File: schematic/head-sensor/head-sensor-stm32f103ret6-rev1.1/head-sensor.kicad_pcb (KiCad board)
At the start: 2 copper layers, 49 parts, among them P1 MICROSD-SDIO-CD, P10 SensorsIn, P11 USART1, P12 SensorsGND, P13 RFID-RC522-MODULE, P14 NRF24L01, P15 HeadLEDs, P16 Power, P2 Vibroengines, P3 NRST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

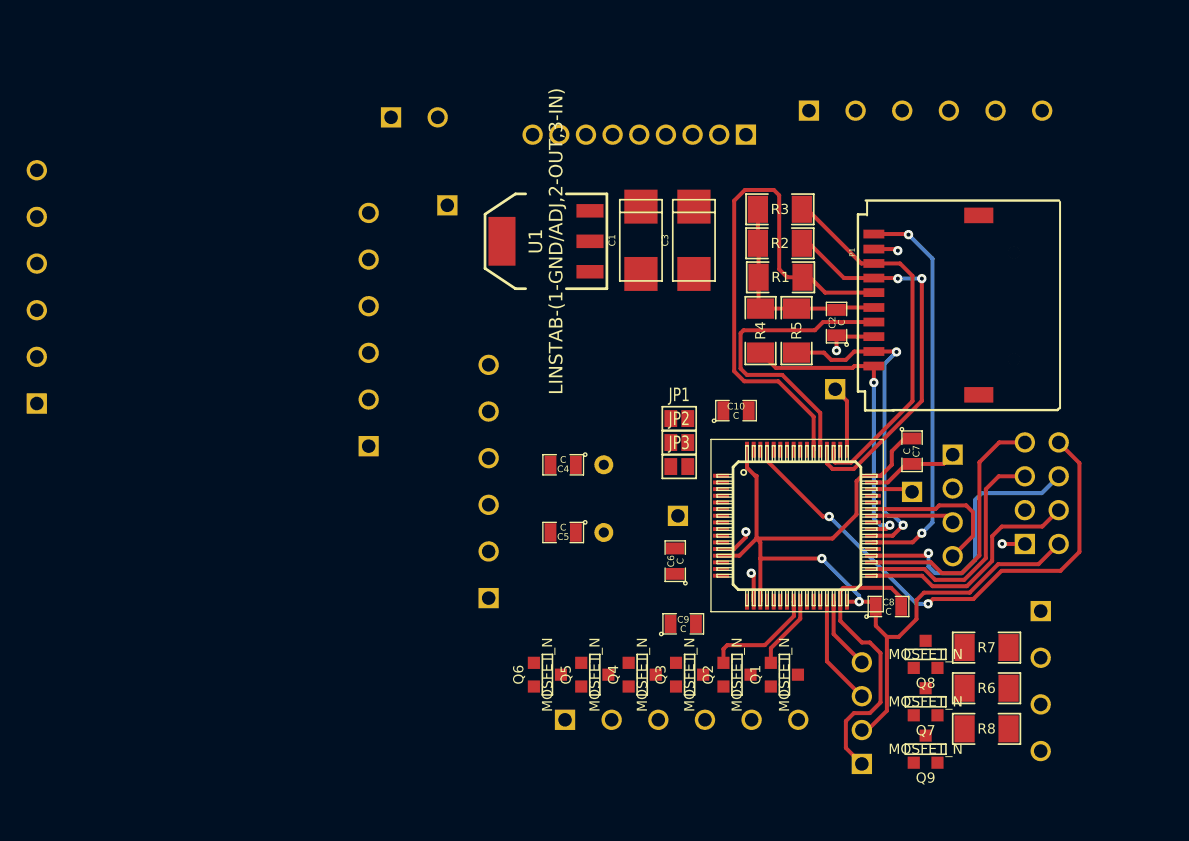
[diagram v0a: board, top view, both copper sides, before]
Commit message: Head sensor routing done
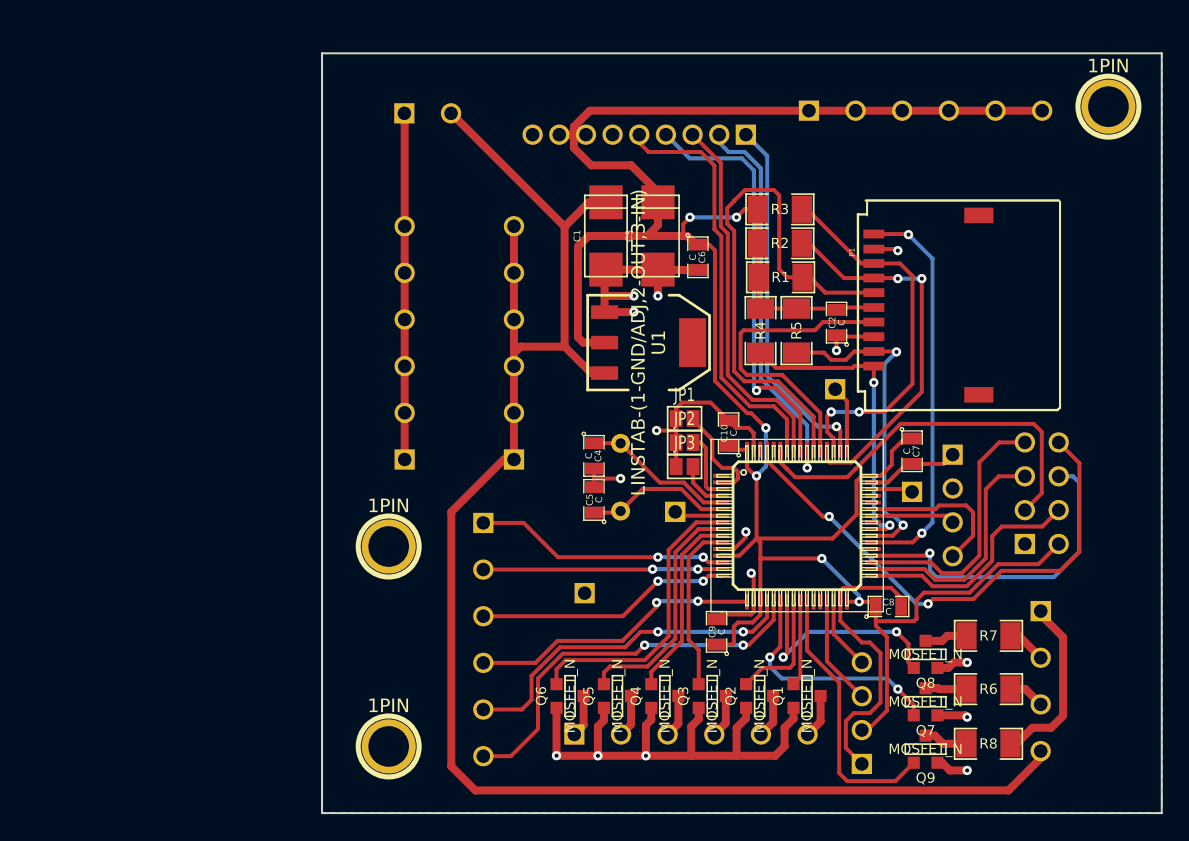
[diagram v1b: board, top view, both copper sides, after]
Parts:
- added 1PIN: P***, 1pin, F.Cu at (127.0, 60.0)
- added 1PIN: P***, 1pin, F.Cu at (73.0, 108.0)
- added 1PIN: P***, 1pin, F.Cu at (73.0, 93.0)
- moved P5 36.0 mm to (82.4, 77.7)
- moved P4 30.9 mm to (87.7, 96.5)
- moved C6 22.9 mm to (96.2, 71.3), turned to 270 degrees
- moved P10 11.9 mm to (80.1, 100.0), turned to 270 degrees
- moved U1 10.8 mm to (92.5, 77.7), turned to 270 degrees
- moved C5 3.36 mm to (88.4, 89.5), turned to 90 degrees
- moved P12 2.88 mm to (74.2, 77.7)
- moved C3 2.72 mm to (93.2, 69.7)
- moved C1 2.65 mm to (89.3, 69.7)
- moved C9 2.57 mm to (97.6, 99.4), turned to 90 degrees
- moved C4 2.40 mm to (88.4, 86.2), turned to 270 degrees
- moved Q1 2.33 mm to (104.4, 104.2)
- moved Q3 2.33 mm to (97.3, 104.2)
- moved Q4 2.33 mm to (93.7, 104.2)
- moved Q5 2.33 mm to (90.2, 104.2)
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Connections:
- C1 pad 2: GND -> AGND
- C10 pad 2: DGND -> AGND
- C2 pad 1: DGND -> AGND
- C3 pad 2: GND -> AGND
- C4 pad 2: DGND -> AGND
- C5 pad 2: DGND -> AGND
- C6 pad 2: DGND -> AGND
- C7 pad 2: DGND -> AGND
- C8 pad 2: DGND -> AGND
- C9 pad 2: DGND -> AGND
- JP1 pad 1: DGND -> AGND
- JP2 pad 1: DGND -> AGND
- JP3 pad 1: DGND -> AGND
- P1 pad 6: DGND -> AGND
- P1 pad CD1: DGND -> AGND
- P11 pad 1: DGND -> AGND
- P12 pad 1: DGND -> AGND
- P12 pad 2: DGND -> AGND
- P12 pad 3: DGND -> AGND
- P12 pad 4: DGND -> AGND
- P12 pad 5: DGND -> AGND
- P12 pad 6: DGND -> AGND
- P13 pad 6: DGND -> AGND
- P14 pad 1: DGND -> AGND
- P4 pad 1: DGND -> AGND
- P6 pad 1: DGND -> AGND
- U1 pad 1: GND -> AGND
- U2 pad 12: DGND -> AGND
- U2 pad 18: DGND -> AGND
- U2 pad 31: DGND -> AGND
- U2 pad 47: DGND -> AGND
- U2 pad 63: DGND -> AGND
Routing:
- net AGND: track 0.00 -> 150.3 mm, vias 0 -> 15
- net +BATT: track 0.00 -> 122.2 mm
- net +3.3V: track 86.7 -> 191.1 mm, vias 2 -> 6
- net DGND: track 41.8 -> 0.00 mm, vias 5 -> 0
- net N-0000021: track 0.00 -> 31.6 mm
- net N-0000022: track 0.00 -> 31.3 mm, vias 0 -> 1
- net N-0000032: track 0.00 -> 29.8 mm, vias 0 -> 1
- net N-0000043: track 0.00 -> 29.6 mm, vias 0 -> 2
- net N-0000027: track 0.00 -> 29.4 mm
- net N-0000023: track 0.00 -> 27.8 mm
- net N-0000031: track 0.00 -> 27.4 mm, vias 0 -> 1
- net N-0000042: track 0.00 -> 26.4 mm, vias 0 -> 2
- net N-0000041: track 0.00 -> 21.9 mm, vias 0 -> 2
- net N-0000015: track 0.00 -> 21.8 mm
- net N-0000045: track 0.00 -> 20.3 mm
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- added copper zone on B.Cu, net AGND
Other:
- board outline added: 63 x 57 mm
- net class Default: trace_width 0.3 -> 0.6
